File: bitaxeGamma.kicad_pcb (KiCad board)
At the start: 4 copper layers, 56.5 x 99.8 mm, 147 parts, among them J1 54-00164, J2 TC2030-IDC, J3 Conn_01x04, J4 Conn_01x06, J5 USB_C_Receptacle_USB2.0, J6 Conn_01x04, J7 Conn_01x04, SW1 GT-TC029B-H025-L1N, SW2 GT-TC029B-H025-L1N, T1 net-tie, U10 EMC2101, U2 TPS546D24ARVFR, U3 RT9080-33GJ5, U4 ESP32-S3-WROOM-1, U5 MCP1824T-1202E/OT, U6 MCP1824T-0802E, U7 25MHz, U8 BM1370_mode1, U9 SN74AVC4T774

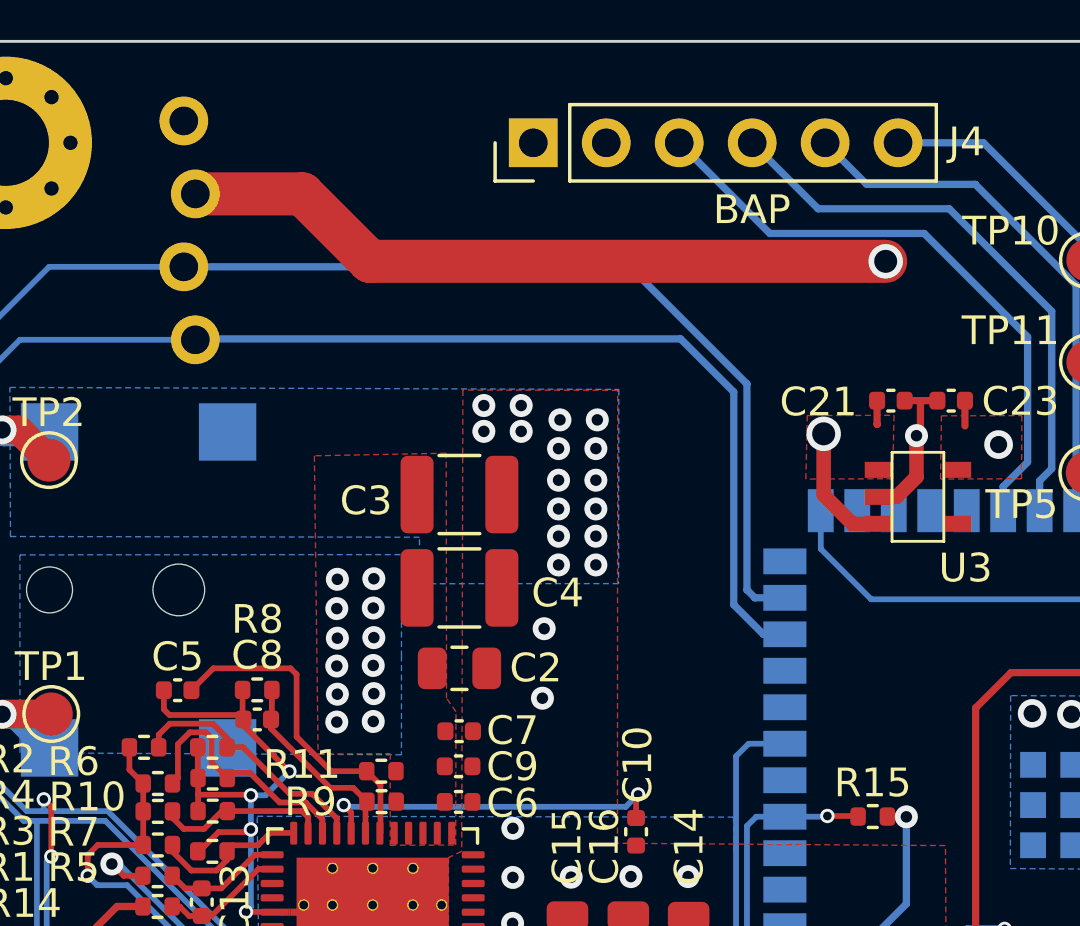
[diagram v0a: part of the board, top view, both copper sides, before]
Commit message: add tps82130 for wide-VIN support
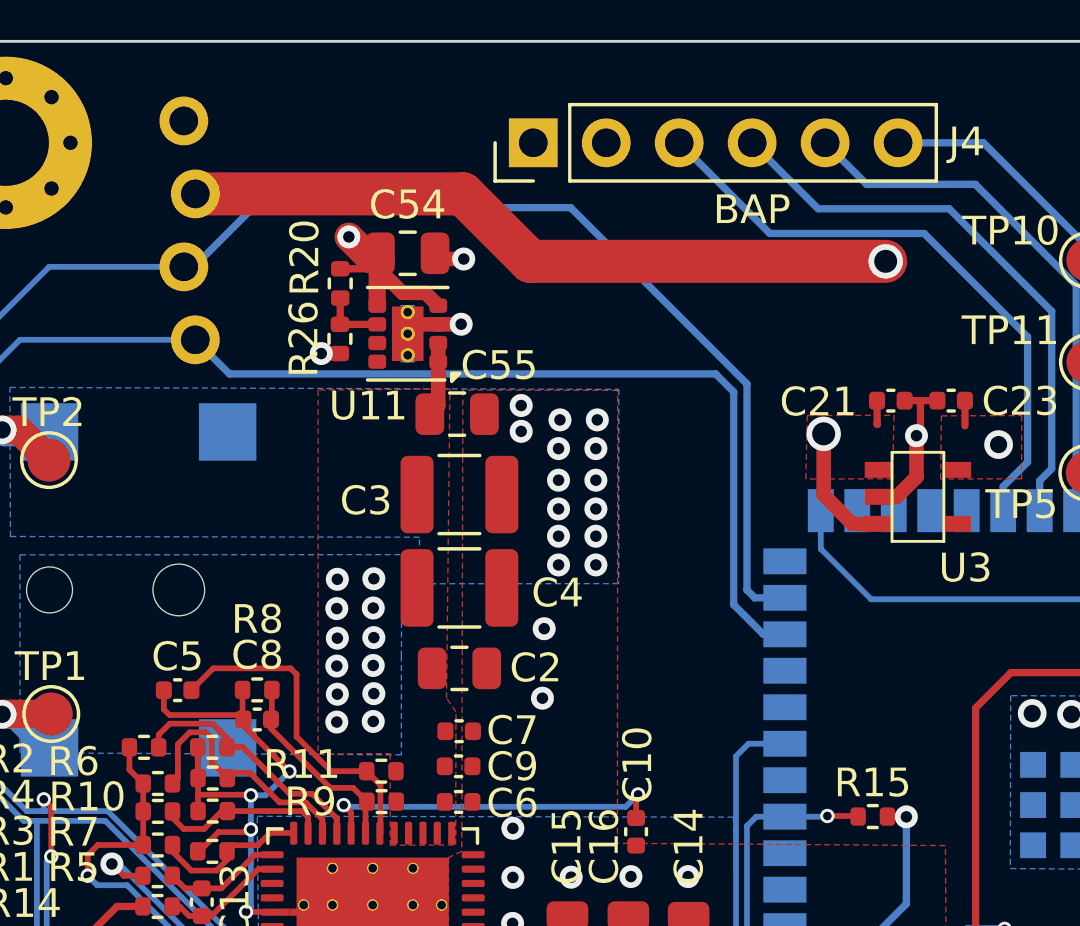
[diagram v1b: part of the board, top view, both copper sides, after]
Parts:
- added C54: 22uF, Capacitor_SMD:C_0805_2012Metric, F.Cu at (94.8, 54.9)
- added C55: 22uF, Capacitor_SMD:C_0805_2012Metric, F.Cu at (96.5, 60.5)
- added R20: 68.1k, Resistor_SMD:R_0402_1005Metric, F.Cu at (92.5, 56.0)
- added R26: 14.7k, Resistor_SMD:R_0402_1005Metric, F.Cu at (92.4, 57.9)
- added U11: TPS82130, Package_LGA:Texas_SIL0008D_MicroSiP-8-1EP_2.8x3mm_P0.65mm_EP1.1x1.9mm_ThermalVias, F.Cu at (94.8, 57.7)
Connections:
- C2 pad 1: /5V -> /Power/VIN
- C3 pad 1: /5V -> /Power/VIN
- C4 pad 1: /5V -> /Power/VIN
- C6 pad 1: /5V -> /Power/VIN
- C7 pad 1: /5V -> /Power/VIN
- C9 pad 1: /5V -> /Power/VIN
- J1 pad 1: /5V -> /Power/VIN
- R11 pad 1: /5V -> /Power/VIN
- R9 pad 1: /5V -> /Power/VIN
- TP1 pad 1: /5V -> /Power/VIN
- U2 pad 21: /5V -> /Power/VIN
- U2 pad 22: /5V -> /Power/VIN
- U2 pad 23: /5V -> /Power/VIN
- U2 pad 24: /5V -> /Power/VIN
- U2 pad 25: /5V -> /Power/VIN
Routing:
- net /Power/VIN: track 0.00 -> 6.44 mm, vias 0 -> 13
- net /5V: track 199.0 -> 202.5 mm, vias 18 -> 6
- net GND: track 100.5 -> 103.4 mm, vias 82 -> 83
- net Net-(U11-FB): track 0.00 -> 2.21 mm
- net /SCL: track 140.3 -> 142.1 mm
- added copper zone on B.Cu, net /Power/VIN
- added copper zone on F.Cu, net /Power/VIN
- removed copper zone on B.Cu, net /5V

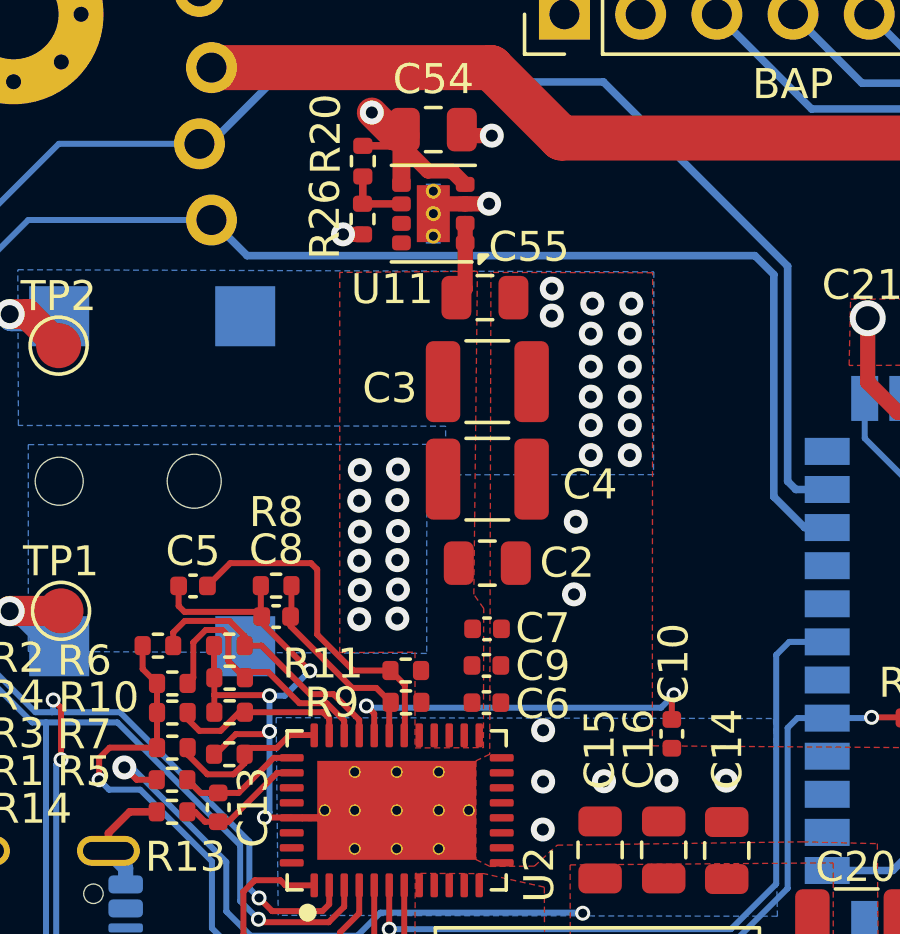
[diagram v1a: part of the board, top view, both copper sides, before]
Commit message: add 0805 0R fallback jumper from VIN->5V
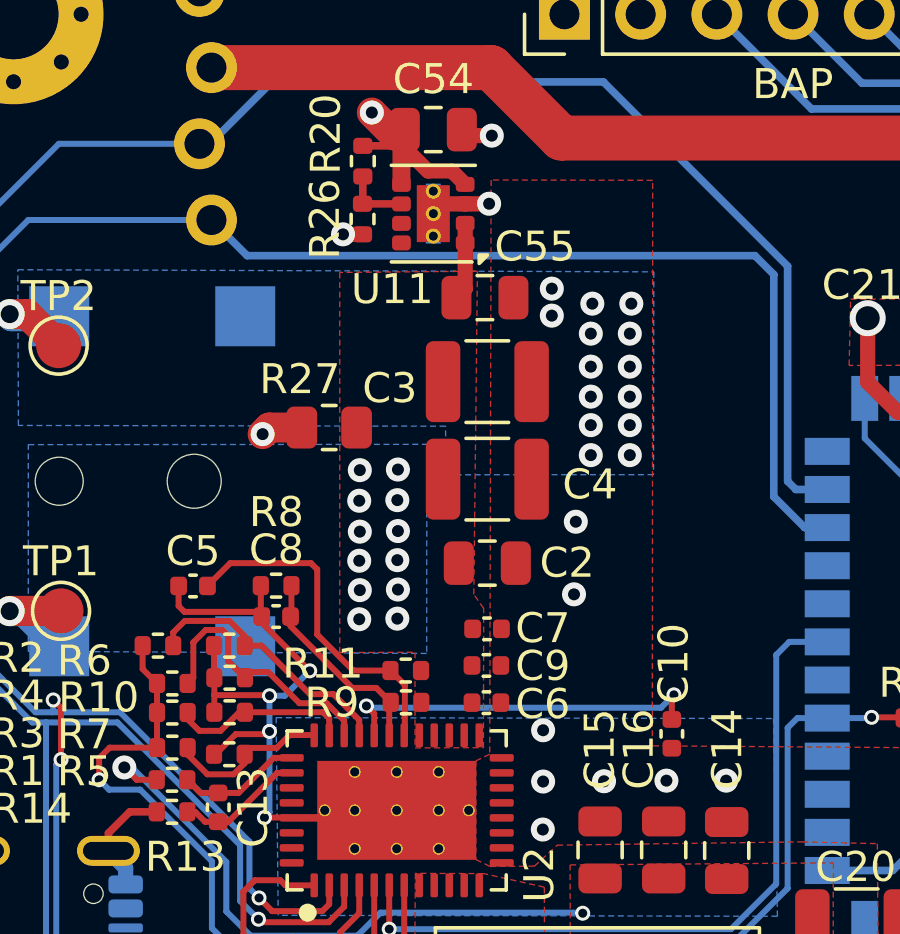
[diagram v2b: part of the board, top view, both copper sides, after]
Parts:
- added R27: 0, Resistor_SMD:R_0805_2012Metric, F.Cu at (91.3, 64.8)
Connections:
- U11 pad 8: (no net) -> unconnected-(U11-SS/TR-Pad8)
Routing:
- net /5V: track 202.5 -> 205.0 mm, vias 6 -> 7

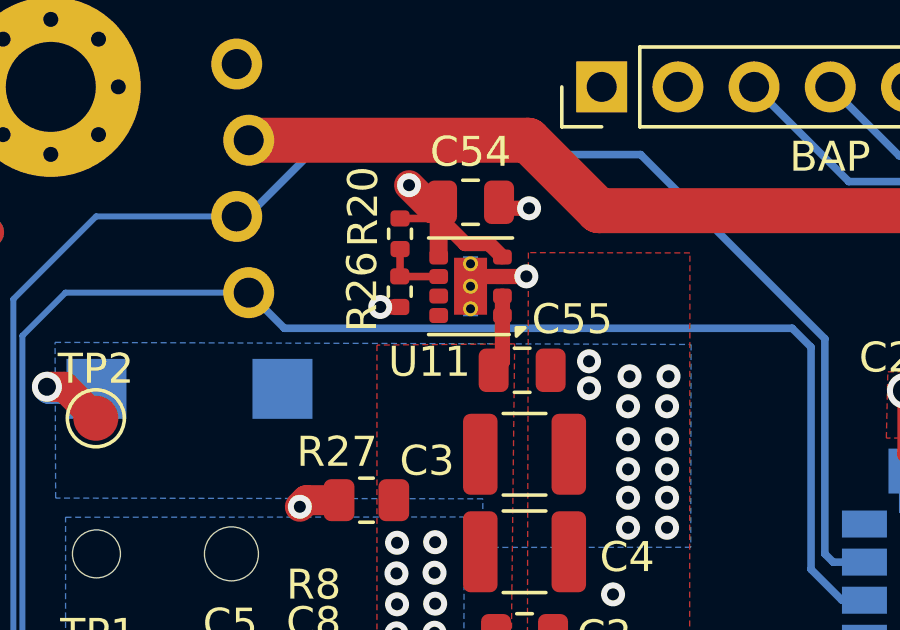
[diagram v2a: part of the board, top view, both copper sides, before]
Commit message: fork sil0008d footprint to fix pad sizes
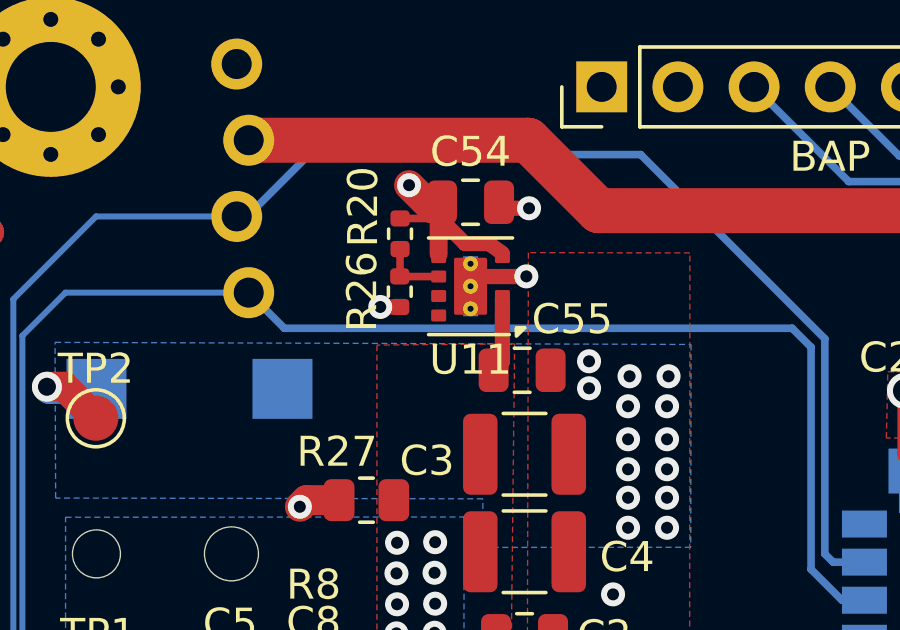
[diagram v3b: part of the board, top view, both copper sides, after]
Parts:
- U11: footprint Package_LGA:Texas_SIL0008D_MicroSiP-8-1EP_2.8x3mm_P0.65mm_EP1.1x1.9mm_ThermalVias -> bitaxe:Texas_SIL0008D_MicroSiP-8-1EP_2.8x3mm_P0.65mm_EP1.1x1.9mm_ThermalVias
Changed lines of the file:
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@@
 		)
 	)
-	(footprint "Package_LGA:Texas_SIL0008D_MicroSiP-8-1EP_2.8x3mm_P0.65mm_EP1.1x1.9mm_ThermalVias"
+	(footprint "bitaxe:Texas_SIL0008D_MicroSiP-8-1EP_2.8x3mm_P0.65mm_EP1.1x1.9mm_ThermalVias"
 		(layer "F.Cu")
 		(at 94.8 57.7 180)
@@
 		(tags "Texas MicroSiP NoLead")
 		(property "Reference" "U11"
-			(at 1.37 -2.52 180)
+			(at 0 -2.45 180)
 			(layer "F.SilkS")
 			(effects
@@
 		(pad "1" smd roundrect
 			(at -1.0625 -0.975 180)
-			(size 0.625 0.5)
+			(size 0.5 0.4)
 			(layers "F.Cu" "F.Mask" "F.Paste")
-			(roundrect_rratio 0.25)
+			(roundrect_rratio 0.125)
 			(net 102 "/Power/VIN")
 			(pinfunction "EN")
@@
 		(pad "2" smd roundrect
 			(at -1.0625 -0.325 180)
-			(size 0.625 0.5)
+			(size 0.5 0.4)
 			(layers "F.Cu" "F.Mask" "F.Paste")
-			(roundrect_rratio 0.25)
+			(roundrect_rratio 0.125)
 			(net 102 "/Power/VIN")
 			(pinfunction "VIN")
@@
 		(pad "3" smd roundrect
 			(at -1.0625 0.325 180)
-			(size 0.625 0.5)
+			(size 0.5 0.4)
 			(layers "F.Cu" "F.Mask" "F.Paste")
-			(roundrect_rratio 0.25)
+			(roundrect_rratio 0.125)
 			(net 1 "GND")
 			(pinfunction "GND")
@@
 		(pad "4" smd roundrect
 			(at -1.0625 0.975 180)
-			(size 0.625 0.5)
+			(size 0.5 0.4)
 			(layers "F.Cu" "F.Mask" "F.Paste")
-			(roundrect_rratio 0.25)
+			(roundrect_rratio 0.125)
 			(net 4 "/5V")
 			(pinfunction "VOUT")
@@
 		(pad "5" smd roundrect
 			(at 1.0625 0.975 180)
-			(size 0.625 0.5)
+			(size 0.5 0.4)
 			(layers "F.Cu" "F.Mask" "F.Paste")
-			(roundrect_rratio 0.25)
+			(roundrect_rratio 0.125)
 			(net 4 "/5V")
 			(pinfunction "VOUT")
@@
 		(pad "6" smd roundrect
 			(at 1.0625 0.325 180)
-			(size 0.625 0.5)
+			(size 0.5 0.4)
 			(layers "F.Cu" "F.Mask" "F.Paste")
-			(roundrect_rratio 0.25)
+			(roundrect_rratio 0.125)
 			(net 103 "Net-(U11-FB)")
 			(pinfunction "FB")
@@
 		(pad "7" smd roundrect
 			(at 1.0625 -0.325 180)
-			(size 0.625 0.5)
+			(size 0.5 0.4)
 			(layers "F.Cu" "F.Mask" "F.Paste")
-			(roundrect_rratio 0.25)
+			(roundrect_rratio 0.125)
 			(net 104 "unconnected-(U11-PG-Pad7)")
 			(pinfunction "PG")
@@
 		(pad "8" smd roundrect
 			(at 1.0625 -0.975 180)
-			(size 0.625 0.5)
+			(size 0.5 0.4)
 			(layers "F.Cu" "F.Mask" "F.Paste")
-			(roundrect_rratio 0.25)
+			(roundrect_rratio 0.125)
 			(net 105 "unconnected-(U11-SS{slash}TR-Pad8)")
 			(pinfunction "SS/TR")
@@
 			(at 0 -0.75 180)
 			(size 0.5 0.5)
-			(drill 0.3)
+			(drill 0.2)
 			(property pad_prop_heatsink)
 			(layers "*.Cu")
@@
 			(at 0 0 180)
 			(size 0.5 0.5)
-			(drill 0.3)
+			(drill 0.2)
 			(property pad_prop_heatsink)
 			(layers "*.Cu")
@@
 			(zone_connect 2)
 		)
-		(pad "9" smd rect
+		(pad "9" smd roundrect
 			(at 0 0 180)
 			(size 1.1 1.9)
 			(property pad_prop_heatsink)
 			(layers "F.Cu" "F.Mask")
+			(roundrect_rratio 0.04545454546)
 			(net 1 "GND")
 			(pinfunction "GND")
@@
 			(at 0 0.75 180)
 			(size 0.5 0.5)
-			(drill 0.3)
+			(drill 0.2)
 			(property pad_prop_heatsink)
 			(layers "*.Cu")
@@
 	)
 	(segment
+		(start 95.8625 56.6)
+		(end 95.4175 56.28)
+		(width 0.5)
+		(layer "F.Cu")
+		(net 4)
+	)
+	(segment
 		(start 94.62 56.28)
 		(end 93.87 55.53)
@@
 	)
 	(segment
-		(start 95.8625 56.725)
-		(end 95.4175 56.28)
-		(width 0.5)
-		(layer "F.Cu")
-		(net 4)
-	)
-	(segment
 		(start 108.741 129.279)
 		(end 109.8435 129.279)
@@
 	(segment
 		(start 95.8625 60.2075)
-		(end 95.8625 58.025)
+		(end 95.8625 58.125)
 		(width 0.508)
 		(layer "F.Cu")
